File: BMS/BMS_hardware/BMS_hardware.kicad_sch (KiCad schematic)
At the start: 24 parts, among them J1 Conn_01x02_Pin, J2 Conn_01x02_Pin, J3 Conn_01x04_Pin, U1 TPS25200DRVR, U3 ICL7660

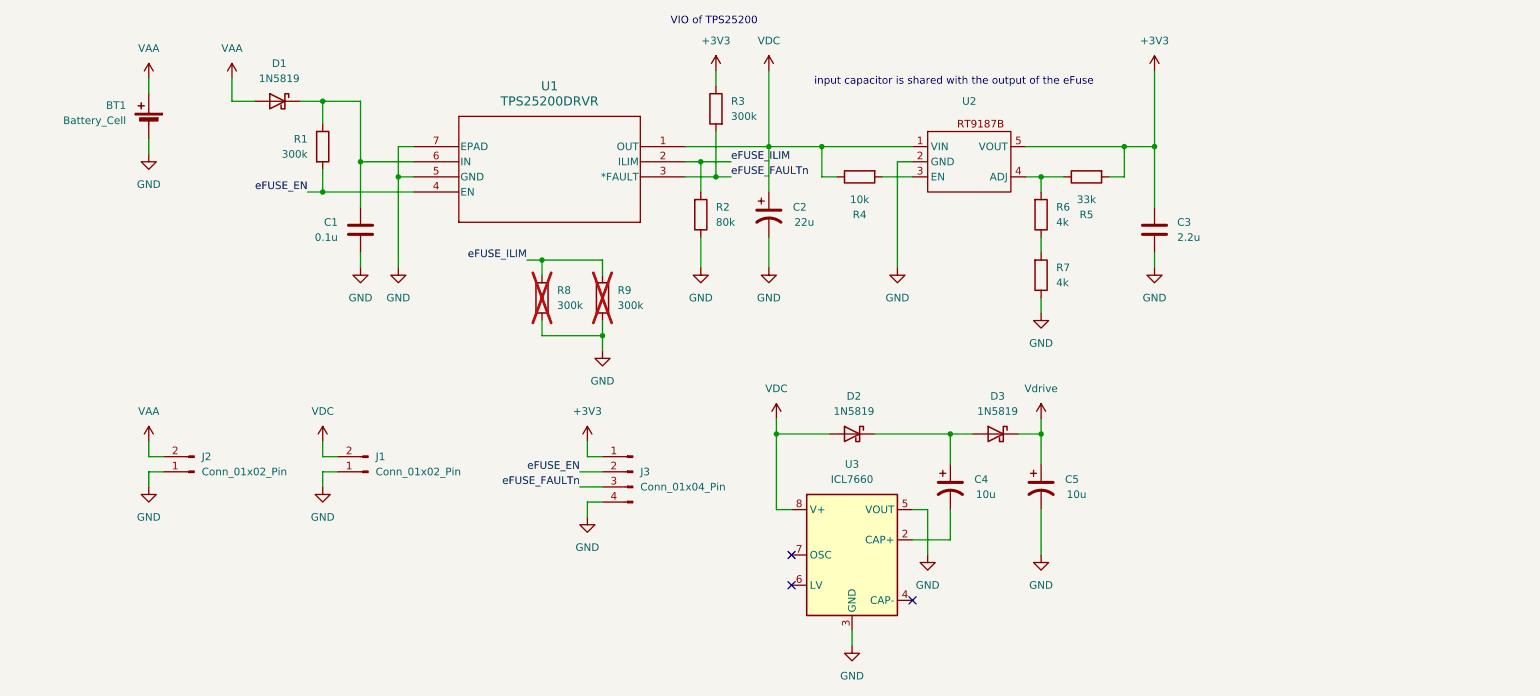
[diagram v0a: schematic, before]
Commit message: Added MAX660 for voltage doubling.
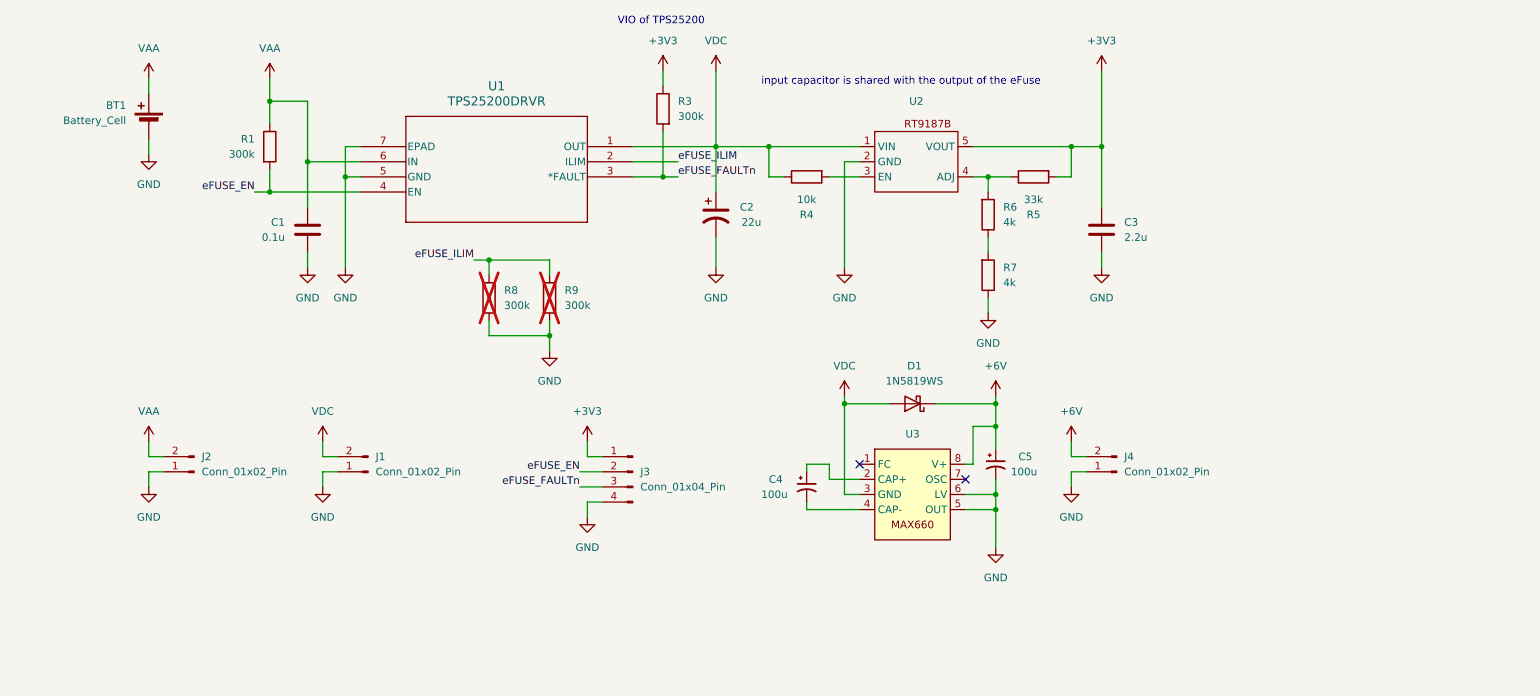
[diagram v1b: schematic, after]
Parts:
- removed C4, C5: 10u, Capacitor_THT:CP_Radial_D6.3mm_P2.50mm, symbol Device:C_Polarized_US
- removed D1, D2, D3: 1N5819, Diode_THT:D_DO-41_SOD81_P10.16mm_Horizontal, symbol Diode:1N5819
- removed R2: 80k, Resistor_SMD:R_0603_1608Metric_Pad0.98x0.95mm_HandSolder, symbol Device:R
- removed U3: ICL7660, symbol Regulator_SwitchedCapacitor:ICL7660
- added C4, C5: 100u, symbol Device:C_Polarized_Small_US
- added D1: 1N5819WS, Diode_SMD:D_SOD-323, symbol Diode:1N5819WS
- added J4: Conn_01x02_Pin, TerminalBlock_Phoenix:TerminalBlock_Phoenix_MKDS-1,5-2-5.08_1x02_P5.08mm_Horizontal, symbol Connector:Conn_01x02_Pin
- added U3: ~, Package_SO:SOIC-8_3.9x4.9mm_P1.27mm, symbol max660:MAX660
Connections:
- net GND: now also C5.2, J4.1 (Pin_1), U3.5 (OUT), U3.6 (LV)
- net VAA: now also C1.1, R1.1, U1.6 (IN)
- net VDC: now also D1.2 (A), U3.3 (GND)
- new net: C4.1, U3.2 (CAP+)
- new net: C4.2, U3.4 (CAP-)
- new net +6V: C5.1, D1.1 (K), J4.2 (Pin_2), U3.8 (V+)
- no-connect marks 3 -> 2
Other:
- moved on the sheet: C1, C2, C3, R1, R3, R4, R5, R6, R7, R8, R9, U1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

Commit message: First schematic version.
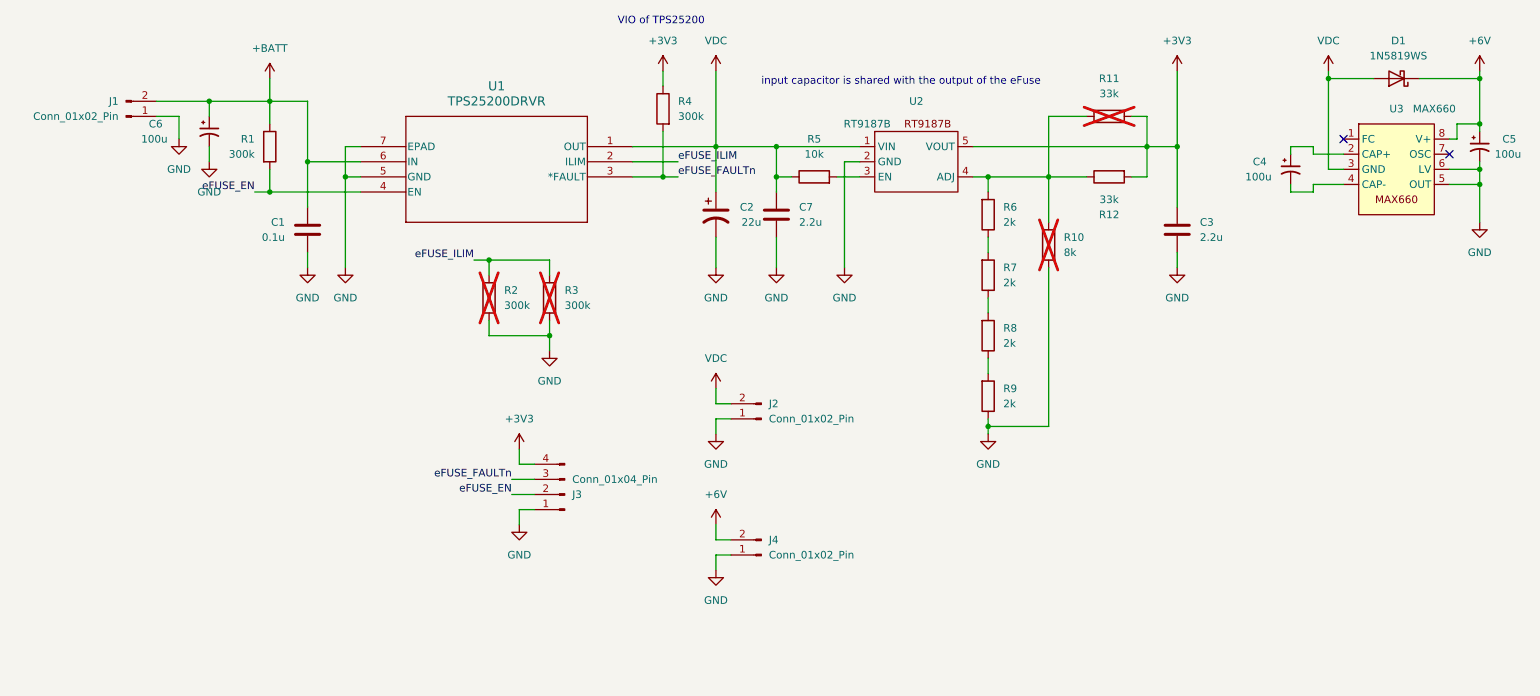
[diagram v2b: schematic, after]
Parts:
- removed BT1: Battery_Cell, Battery:BatteryHolder_MPD_BH-18650-PC2, symbol Device:Battery_Cell
- removed J2: Conn_01x02_Pin, TerminalBlock_Phoenix:TerminalBlock_Phoenix_MKDS-1,5-2-5.08_1x02_P5.08mm_Horizontal, symbol Connector:Conn_01x02_Pin
- added C6: 100u, Capacitor_THT:CP_Radial_D6.3mm_P2.50mm, symbol Device:C_Polarized_Small_US
- added C7: 2.2u, Capacitor_SMD:C_0805_2012Metric_Pad1.18x1.45mm_HandSolder, symbol Device:C
- added J1: Conn_01x02_Pin, TerminalBlock_Phoenix:TerminalBlock_Phoenix_MKDS-1,5-2-5.08_1x02_P5.08mm_Horizontal, symbol Connector:Conn_01x02_Pin
- added R10: 8k, Resistor_THT:R_Axial_DIN0207_L6.3mm_D2.5mm_P7.62mm_Horizontal, symbol Device:R
- added R11: 33k, Resistor_THT:R_Axial_DIN0207_L6.3mm_D2.5mm_P7.62mm_Horizontal, symbol Device:R
- added R8, R9: 2k, Resistor_SMD:R_0603_1608Metric_Pad0.98x0.95mm_HandSolder, symbol Device:R
- C1: footprint Capacitor_SMD:C_1206_3216Metric_Pad1.33x1.80mm_HandSolder -> Capacitor_SMD:C_0603_1608Metric_Pad1.08x0.95mm_HandSolder; LCSC (none) -> C14663
- C2, J4: now left out of the parts list
- C3: LCSC (none) -> C377773
- C4, C5: footprint (none) -> Capacitor_THT:CP_Radial_D6.3mm_P2.50mm; now left out of the parts list
- D1: LCSC (none) -> C191023
- J2: renamed from J1; now left out of the parts list
- J3: footprint (none) -> Connector_PinHeader_2.54mm:PinHeader_1x04_P2.54mm_Vertical; now left out of the parts list
- R1: LCSC (none) -> C23024
- R12: renamed from R5; footprint (none) -> Resistor_SMD:R_0603_1608Metric_Pad0.98x0.95mm_HandSolder; LCSC (none) -> C4216
- R4: renamed from R3; LCSC (none) -> C23024
- R5: renamed from R4; footprint (none) -> Resistor_SMD:R_0603_1608Metric_Pad0.98x0.95mm_HandSolder; LCSC (none) -> C25804
- R6, R7: value 4k -> 2k; LCSC (none) -> C22975
- U1: footprint tps25200:DRV6_1X1P6_TEX -> Package_SON:WSON-6-1EP_2x2mm_P0.65mm_EP1x1.6mm_ThermalVias; LCSC (none) -> C128401
- U2: value ~ -> RT9187B; LCSC (none) -> C3031681
- U3: value ~ -> MAX660; now left out of the parts list
- renumbered R8 to R2, R9 to R3
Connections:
- net +3V3: now also J3.4 (Pin_4), R11.2; no longer J3.1 (Pin_1)
- net GND: now also J3.1 (Pin_1), C6.2, C7.2, J1.1 (Pin_1), R10.2, R9.1; no longer J3.4 (Pin_4), R7.1
- net VDC: now also C7.1
- net at R12.1, R6.2, U2.4 (ADJ): now also R10.1, R11.1
- net VAA renamed +BATT
- net +BATT: now also C6.1, J1.2 (Pin_2)
- new net: R8.1, R9.2
- new net: R7.1, R8.2
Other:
- moved on the sheet: C3, C4, C5, D1, J2, J4, R12, R5, U3
